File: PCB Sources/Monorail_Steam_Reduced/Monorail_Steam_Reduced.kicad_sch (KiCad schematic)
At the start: 134 parts, among them J6 USB_C_Receptacle_USB2.0, J8 Conn_01x04_Male, J9 Conn_01x03_Male, SW3 RotaryEncoder_Switch, U1 SRV05-4, U2 XC6206PxxxMR, U3 RP2040TR7, U4 W25Q128JVS, Y1 Crystal_GND24_Small

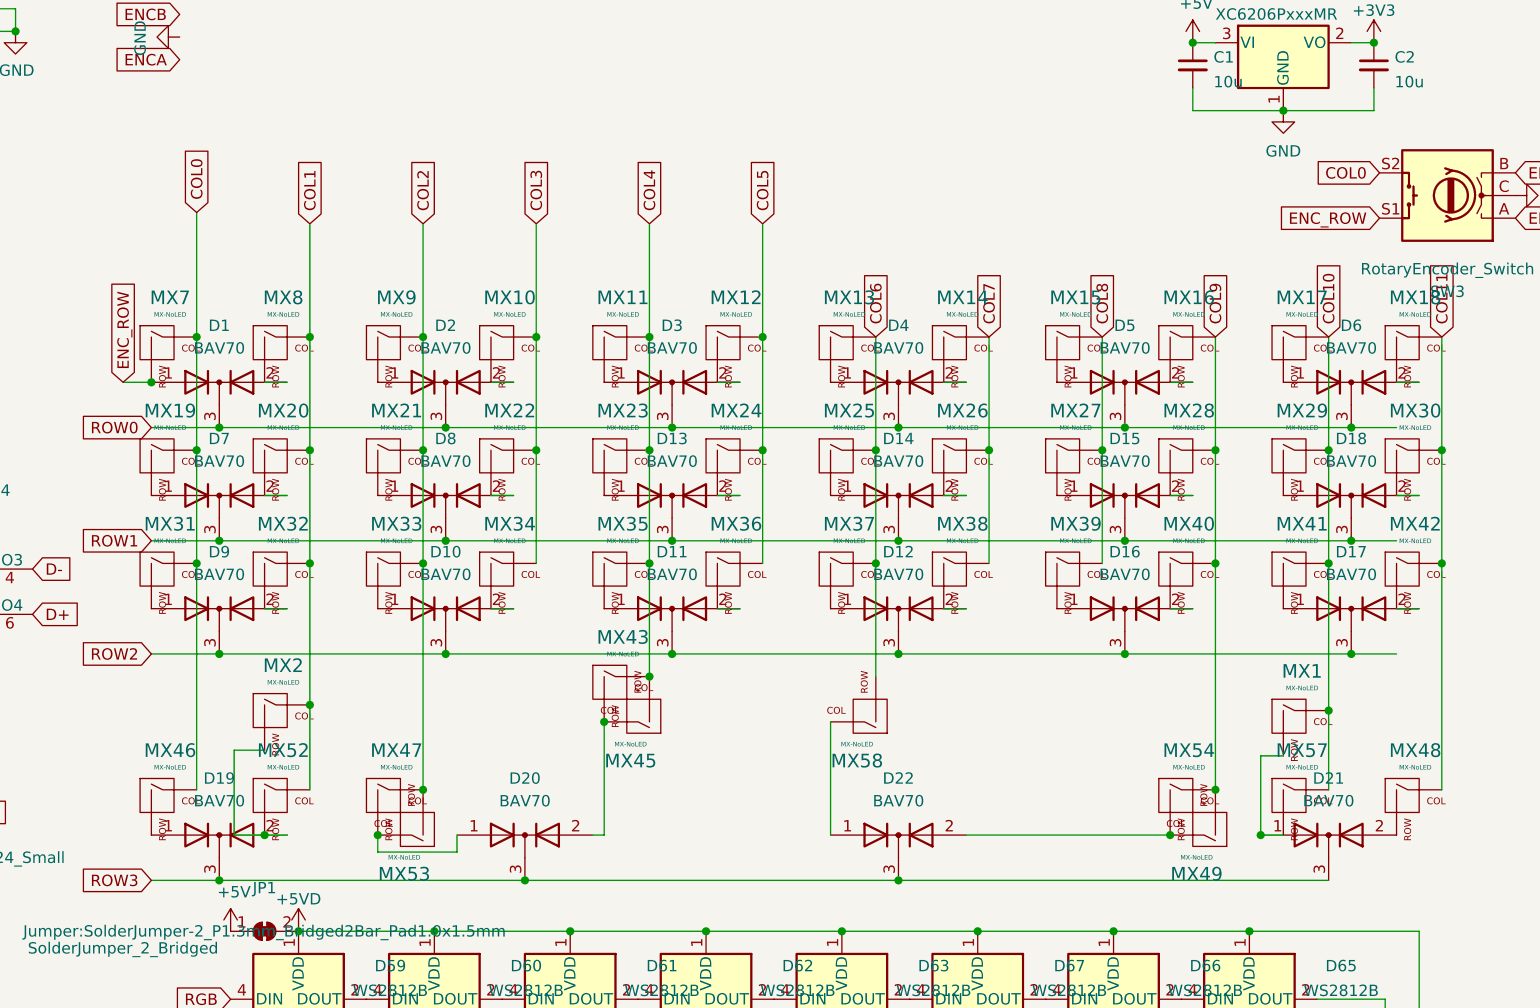
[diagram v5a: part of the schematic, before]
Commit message: updated routing, position of diodes
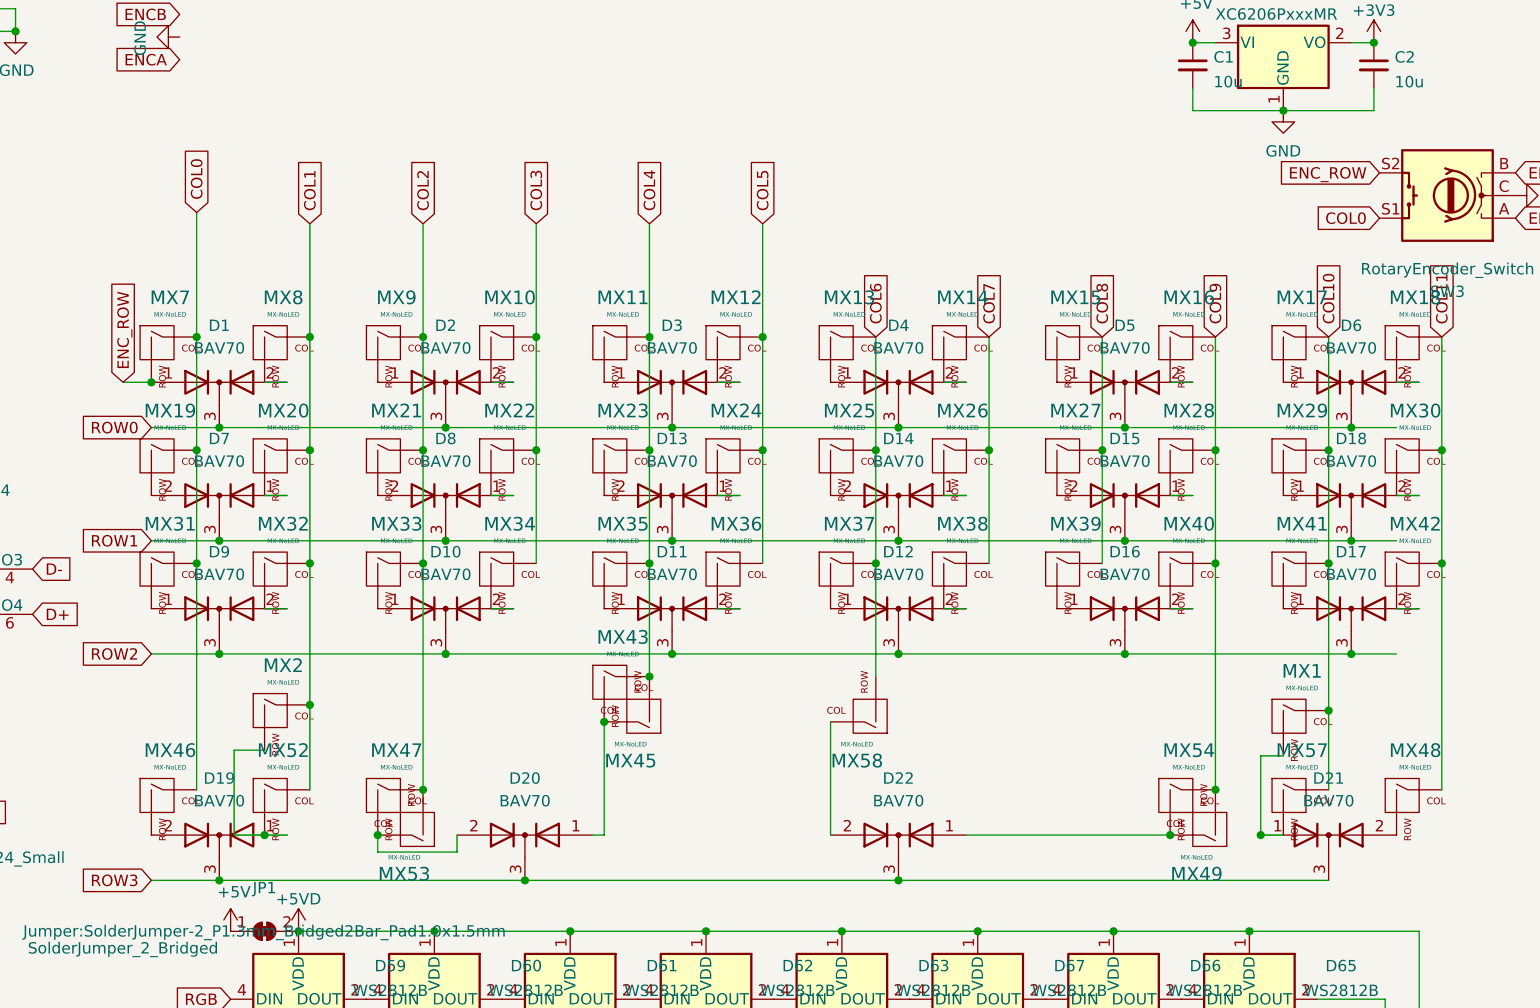
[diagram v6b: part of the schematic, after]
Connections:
- net COL0: now also SW3.S1; no longer SW3.S2
- net ENC_ROW: now also SW3.S2; no longer SW3.S1
- net at MX49.1 (COL), MX54.2 (ROW): now also D22.1 (A); no longer D22.2 (A)
- net at MX19.2 (ROW): now also D7.2 (A); no longer D7.1 (A)
- net at MX20.2 (ROW): now also D7.1 (A); no longer D7.2 (A)
- net at MX21.2 (ROW): now also D8.2 (A); no longer D8.1 (A)
- net at MX22.2 (ROW): now also D8.1 (A); no longer D8.2 (A)
- net at MX23.2 (ROW): now also D13.2 (A); no longer D13.1 (A)
- net at MX24.2 (ROW): now also D13.1 (A); no longer D13.2 (A)
- net at MX25.2 (ROW): now also D14.2 (A); no longer D14.1 (A)
- net at MX26.2 (ROW): now also D14.1 (A); no longer D14.2 (A)
- net at MX27.2 (ROW): now also D15.2 (A); no longer D15.1 (A)
- net at MX28.2 (ROW): now also D15.1 (A); no longer D15.2 (A)
- net at MX46.2 (ROW): now also D19.2 (A); no longer D19.1 (A)
- net at MX2.2 (ROW), MX52.2 (ROW): now also D19.1 (A); no longer D19.2 (A)
- net at MX47.2 (ROW), MX53.1 (COL): now also D20.2 (A); no longer D20.1 (A)
- net at MX43.2 (ROW), MX45.1 (COL): now also D20.1 (A); no longer D20.2 (A)
- net at MX58.1 (COL): now also D22.2 (A); no longer D22.1 (A)
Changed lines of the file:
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@@
     )
   )
-  (global_label "COL0" (shape input) (at 272.415 45.085 180) (fields_autoplaced)
+  (global_label "COL0" (shape input) (at 272.415 50.165 180) (fields_autoplaced)
     (effects (font (size 1.27 1.27)) (justify right))
-    (property "Intersheetrefs" "${INTERSHEET_REFS}" (at 265.2459 45.085 0)
+    (property "Intersheetrefs" "${INTERSHEET_REFS}" (at 265.2459 50.165 0)
       (effects (font (size 1.27 1.27)) (justify right) hide)
     )
@@
     )
   )
-  (global_label "ENC_ROW" (shape input) (at 272.415 50.165 180) (fields_autoplaced)
+  (global_label "ENC_ROW" (shape input) (at 272.415 45.085 180) (fields_autoplaced)
     (effects (font (size 1.27 1.27)) (justify right))
-    (property "Intersheetrefs" "${INTERSHEET_REFS}" (at 261.315 50.165 0)
+    (property "Intersheetrefs" "${INTERSHEET_REFS}" (at 261.315 45.085 0)
       (effects (font (size 1.27 1.27)) (justify right) hide)
     )
@@
     )
   )
-  (symbol (lib_id "Diode:BAV70") (at 193.04 81.28 0) (unit 1)
-    (in_bom yes) (on_board yes) (dnp no) (fields_autoplaced)
+  (symbol (lib_id "Diode:BAV70") (at 193.04 81.28 0) (mirror y) (unit 1)
+    (in_bom yes) (on_board yes) (dnp no)
     (property "Reference" "D13" (at 193.04 74.93 0)
       (effects (font (size 1.27 1.27)))
@@
     )
   )
-  (symbol (lib_id "Diode:BAV70") (at 167.64 81.28 0) (unit 1)
-    (in_bom yes) (on_board yes) (dnp no) (fields_autoplaced)
+  (symbol (lib_id "Diode:BAV70") (at 167.64 81.28 0) (mirror y) (unit 1)
+    (in_bom yes) (on_board yes) (dnp no)
     (property "Reference" "D8" (at 167.64 74.93 0)
       (effects (font (size 1.27 1.27)))
@@
     )
   )
-  (symbol (lib_id "Diode:BAV70") (at 142.24 81.28 0) (unit 1)
-    (in_bom yes) (on_board yes) (dnp no) (fields_autoplaced)
+  (symbol (lib_id "Diode:BAV70") (at 142.24 81.28 0) (mirror y) (unit 1)
+    (in_bom yes) (on_board yes) (dnp no)
     (property "Reference" "D7" (at 142.24 74.93 0)
       (effects (font (size 1.27 1.27)))
@@
     )
   )
-  (symbol (lib_id "Diode:BAV70") (at 218.44 81.28 0) (unit 1)
-    (in_bom yes) (on_board yes) (dnp no) (fields_autoplaced)
+  (symbol (lib_id "Diode:BAV70") (at 218.44 81.28 0) (mirror y) (unit 1)
+    (in_bom yes) (on_board yes) (dnp no)
     (property "Reference" "D14" (at 218.44 74.93 0)
       (effects (font (size 1.27 1.27)))
@@
     )
   )
-  (symbol (lib_id "Diode:BAV70") (at 142.24 119.38 0) (unit 1)
-    (in_bom yes) (on_board yes) (dnp no) (fields_autoplaced)
+  (symbol (lib_id "Diode:BAV70") (at 142.24 119.38 0) (mirror y) (unit 1)
+    (in_bom yes) (on_board yes) (dnp no)
     (property "Reference" "D19" (at 142.24 113.03 0)
       (effects (font (size 1.27 1.27)))
@@
     )
   )
-  (symbol (lib_id "Diode:BAV70") (at 176.53 119.38 0) (unit 1)
-    (in_bom yes) (on_board yes) (dnp no) (fields_autoplaced)
+  (symbol (lib_id "Diode:BAV70") (at 176.53 119.38 0) (mirror y) (unit 1)
+    (in_bom yes) (on_board yes) (dnp no)
     (property "Reference" "D20" (at 176.53 113.03 0)
       (effects (font (size 1.27 1.27)))
@@
     )
   )
-  (symbol (lib_id "Diode:BAV70") (at 218.44 119.38 0) (unit 1)
-    (in_bom yes) (on_board yes) (dnp no) (fields_autoplaced)
+  (symbol (lib_id "Diode:BAV70") (at 218.44 119.38 0) (mirror y) (unit 1)
+    (in_bom yes) (on_board yes) (dnp no)
     (property "Reference" "D22" (at 218.44 113.03 0)
       (effects (font (size 1.27 1.27)))
@@
     )
   )
-  (symbol (lib_id "Diode:BAV70") (at 243.84 81.28 0) (unit 1)
-    (in_bom yes) (on_board yes) (dnp no) (fields_autoplaced)
+  (symbol (lib_id "Diode:BAV70") (at 243.84 81.28 0) (mirror y) (unit 1)
+    (in_bom yes) (on_board yes) (dnp no)
     (property "Reference" "D15" (at 243.84 74.93 0)
       (effects (font (size 1.27 1.27)))

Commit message: finished base routing
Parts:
- removed C24: 100n, Capacitor_SMD:C_0402_1005Metric, symbol Device:C_Small
- removed D53, D54, D55: LED, LED_THT:LED_D3.0mm, symbol Device:LED
- removed R10, R11, R9: 470, Resistor_SMD:R_0603_1608Metric, symbol Device:R_Small
- added J1, J2, J3: Conn_01x02_Male, Connector_PinHeader_2.54mm:PinHeader_1x02_P2.54mm_Vertical, symbol Connector:Conn_01x02_Male
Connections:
- net +3V3: now also J8.2 (Pin_2)
- net +5V: now also C13.1, C14.1, C15.1, C16.1, C17.1, C18.1, C19.1, C20.1; no longer J8.2 (Pin_2)
- net +5VD: no longer C13.1, C14.1, C15.1, C16.1, C17.1, C18.1, C19.1, C20.1
- net COL0: now also U3.37 (GPIO25); no longer U3.35 (GPIO23)
- net COL1: now also U3.36 (GPIO24); no longer U3.34 (GPIO22)
- net COL10: now also U3.14 (GPIO11); no longer U3.8 (GPIO6)
- net COL11: now also U3.6 (GPIO4); no longer U3.2 (GPIO0)
- net COL2: now also U3.35 (GPIO23); no longer U3.32 (GPIO21)
- net COL3: now also U3.29 (GPIO18); no longer U3.31 (GPIO20)
- net COL4: now also U3.7 (GPIO5); no longer U3.30 (GPIO19)
- net COL5: now also U3.8 (GPIO6); no longer U3.29 (GPIO18)
- net COL6: now also U3.9 (GPIO7); no longer U3.28 (GPIO17)
- net COL7: now also U3.18 (GPIO15); no longer U3.27 (GPIO16)
- net COL8: now also U3.16 (GPIO13); no longer U3.13 (GPIO10)
- net COL9: now also U3.17 (GPIO14); no longer U3.14 (GPIO11)
- net ENCA: now also U3.39 (GPIO27/ADC1); no longer U3.15 (GPIO12)
- net ENCB: now also U3.40 (GPIO28/ADC2); no longer U3.36 (GPIO24)
- net GND: now also J1.2 (Pin_2), J2.2 (Pin_2), J3.2 (Pin_2)
- net LED1: now also U3.13 (GPIO10), J1.1 (Pin_1); no longer U3.37 (GPIO25)
- net LED2: now also U3.11 (GPIO8), J2.1 (Pin_1); no longer U3.38 (GPIO26/ADC0)
- net LED3: now also U3.12 (GPIO9), J3.1 (Pin_1); no longer U3.39 (GPIO27/ADC1)
- net RGB: no longer U3.41 (GPIO29/ADC3)
- net ROW0: now also U3.41 (GPIO29/ADC3); no longer U3.12 (GPIO9)
- net ROW1: now also U3.38 (GPIO26/ADC0); no longer U3.3 (GPIO1)
- net ROW2: now also U3.15 (GPIO12); no longer U3.6 (GPIO4)
- net ROW3: no longer U3.7 (GPIO5)
- net ROW4: no longer U3.40 (GPIO28/ADC2)
- net SCL: now also U3.4 (GPIO2); no longer U3.5 (GPIO3)
- net SDA: now also U3.5 (GPIO3); no longer U3.4 (GPIO2)
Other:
- moved on the sheet: H1
